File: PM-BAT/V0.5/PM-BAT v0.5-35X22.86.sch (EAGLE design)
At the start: 87 parts, among them J1 M13PTH-CST-R, J2 M12PTH-CST-R, U1 BQ24195, U2 TPS63020, U3 TPS631011, U5 TPS22918, U6 SPARKFUN-POWERIC_MAX1704X

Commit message: update
update  and output DXF for DFM
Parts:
- added R18: 10K, particle SZ:RESR0201-N
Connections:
- net ENABLE: now also R18.2
- net N$21: now also R18.1
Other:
- moved on the sheet: C23, C26, C27, C29

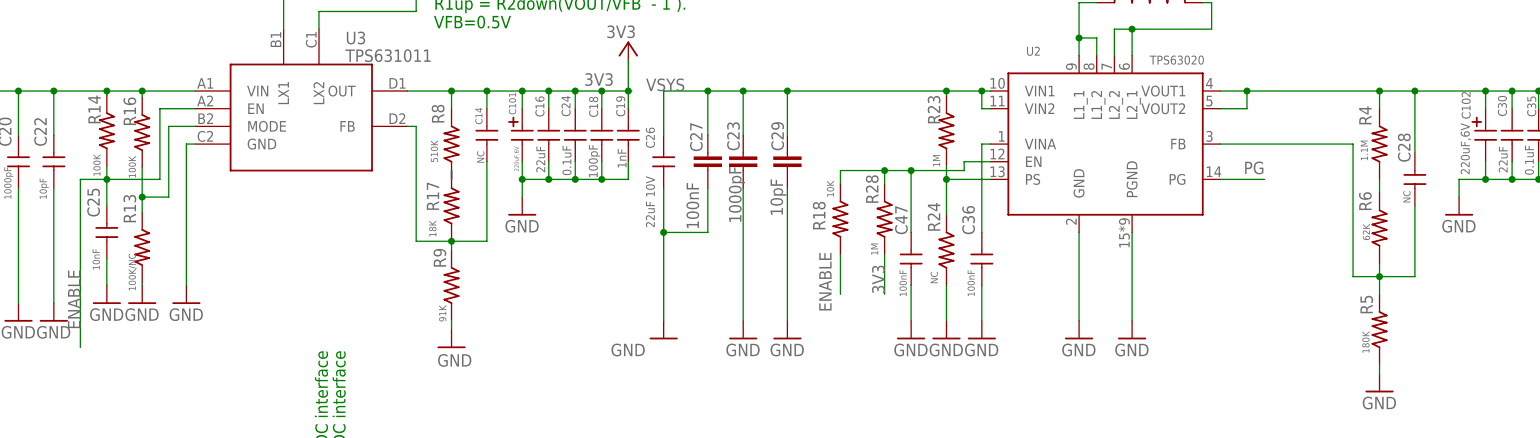
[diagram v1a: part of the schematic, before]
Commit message: upload xydate and placement and update based test
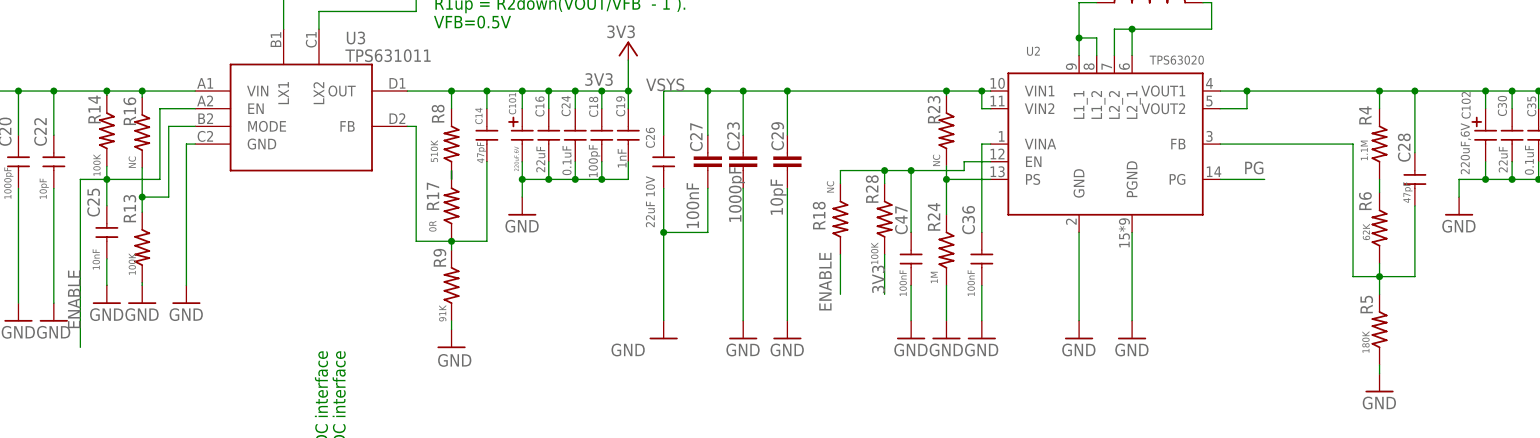
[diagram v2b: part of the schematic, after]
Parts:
- C14, C28: value NC -> 47pF
- R13: value 100K/NC -> 100K
- R16: value 100K -> NC
- R17: value 18K -> 0R
- R18: value 10K -> NC
- R23: value 1M -> NC
- R24: value NC -> 1M
- R28: value 1M -> 100K
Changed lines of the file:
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@@
 <attribute name="ITEM_NUMBER" value=""/>
 </part>
-<part name="R17" library="particle SZ" deviceset="RES" device="R0201-N" value="18K">
+<part name="R17" library="particle SZ" deviceset="RES" device="R0201-N" value="0R">
 <attribute name="ITEM_NAME" value="RES SMD 24K OHM 1% 1/16W 0402"/>
 <attribute name="ITEM_NUMBER" value="PT-201025"/>
@@
 </part>
 <part name="GND18" library="supply1" deviceset="GND" device=""/>
-<part name="R23" library="particle SZ" deviceset="RES" device="R0201-N" value="1M">
-<attribute name="ITEM_NAME" value="RES SMD 1M OHM 1% 1/16W 0402"/>
-<attribute name="ITEM_NUMBER" value="PT-201084"/>
-</part>
-<part name="R24" library="particle SZ" deviceset="RES" device="R0201-N" value="NC">
+<part name="R23" library="particle SZ" deviceset="RES" device="R0201-N" value="NC">
+<attribute name="ITEM_NAME" value="RES SMD 1M OHM 1% 1/16W 0402"/>
+<attribute name="ITEM_NUMBER" value="PT-201084"/>
+</part>
+<part name="R24" library="particle SZ" deviceset="RES" device="R0201-N" value="1M">
 <attribute name="ITEM_NAME" value=""/>
 <attribute name="ITEM_NUMBER" value=""/>
@@
 <part name="GND27" library="supply1" deviceset="GND" device=""/>
 <part name="GND28" library="supply1" deviceset="GND" device=""/>
-<part name="R28" library="particle SZ" deviceset="RES" device="R0201-N" value="1M">
+<part name="R28" library="particle SZ" deviceset="RES" device="R0201-N" value="100K">
 <attribute name="ITEM_NAME" value=""/>
 <attribute name="ITEM_NUMBER" value=""/>
@@
 </part>
 <part name="GND32" library="supply1" deviceset="GND" device=""/>
-<part name="C28" library="particle SZ" deviceset="CAP" device="C0201-N" value="NC">
+<part name="C28" library="particle SZ" deviceset="CAP" device="C0201-N" value="47pF">
 <attribute name="ITEM_NAME" value="CAP CER 10uF 6.3V X5R 0603 10% Low ESR&lt;70mohms"/>
 <attribute name="ITEM_NUMBER" value="PT-200209"/>
@@
 <attribute name="ITEM_NUMBER" value="PT-200209"/>
 </part>
-<part name="C14" library="particle SZ" deviceset="CAP" device="C0201-N" value="NC">
+<part name="C14" library="particle SZ" deviceset="CAP" device="C0201-N" value="47pF">
 <attribute name="ITEM_NAME" value="CAP CER 10uF 6.3V X5R 0603 10% Low ESR&lt;70mohms"/>
 <attribute name="ITEM_NUMBER" value="PT-200209"/>
 </part>
 <part name="U1" library="ELEKTRA-PMIC v0.3-35X22.86-0.8-0402" deviceset="ELECTRON_BQ24298RTWR" device="" value="BQ24195"/>
-<part name="R16" library="particle SZ" deviceset="RES" device="R0201-N" value="100K">
-<attribute name="ITEM_NAME" value="RES SMD 1M OHM 1% 1/16W 0402"/>
-<attribute name="ITEM_NUMBER" value="PT-201084"/>
-</part>
-<part name="R13" library="particle SZ" deviceset="RES" device="R0201-N" value="100K/NC">
+<part name="R16" library="particle SZ" deviceset="RES" device="R0201-N" value="NC">
+<attribute name="ITEM_NAME" value="RES SMD 1M OHM 1% 1/16W 0402"/>
+<attribute name="ITEM_NUMBER" value="PT-201084"/>
+</part>
+<part name="R13" library="particle SZ" deviceset="RES" device="R0201-N" value="100K">
 <attribute name="ITEM_NAME" value="RES SMD 1M OHM 1% 1/16W 0402"/>
 <attribute name="ITEM_NUMBER" value="PT-201084"/>
@@
 <attribute name="ITEM_NUMBER" value="120-00060"/>
 </part>
-<part name="R18" library="particle SZ" deviceset="RES" device="R0201-N" value="10K">
-<attribute name="ITEM_NAME" value=""/>
-<attribute name="ITEM_NUMBER" value=""/>
+<part name="R18" library="particle SZ" deviceset="RES" device="R0201-N" value="NC">
+<attribute name="ITEM_NAME" value=""/>
+<attribute name="ITEM_NUMBER" value=""/>
